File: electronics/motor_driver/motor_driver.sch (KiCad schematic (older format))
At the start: 6 parts, among them J101 CONN_02X20, J102 CONN_01X02, J103 CONN_01X02, J104 CONN_01X02

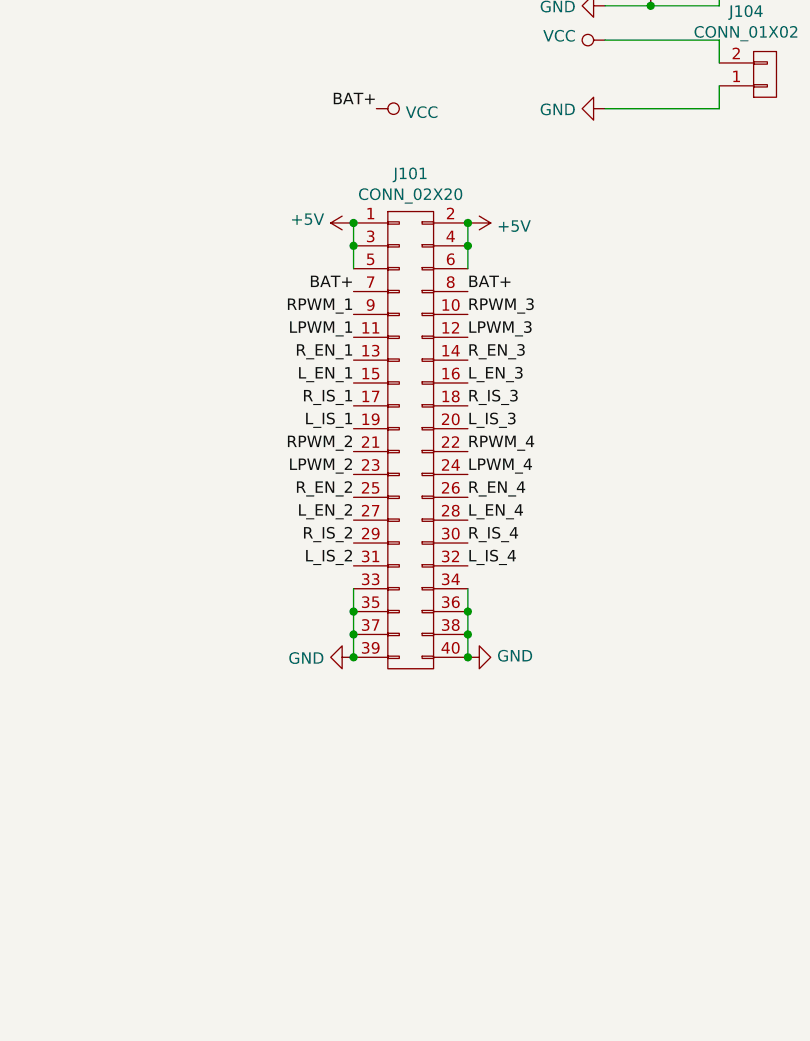
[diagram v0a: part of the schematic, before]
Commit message: Rensa + byta footprints + ändra vior + uppdatera kontakt.
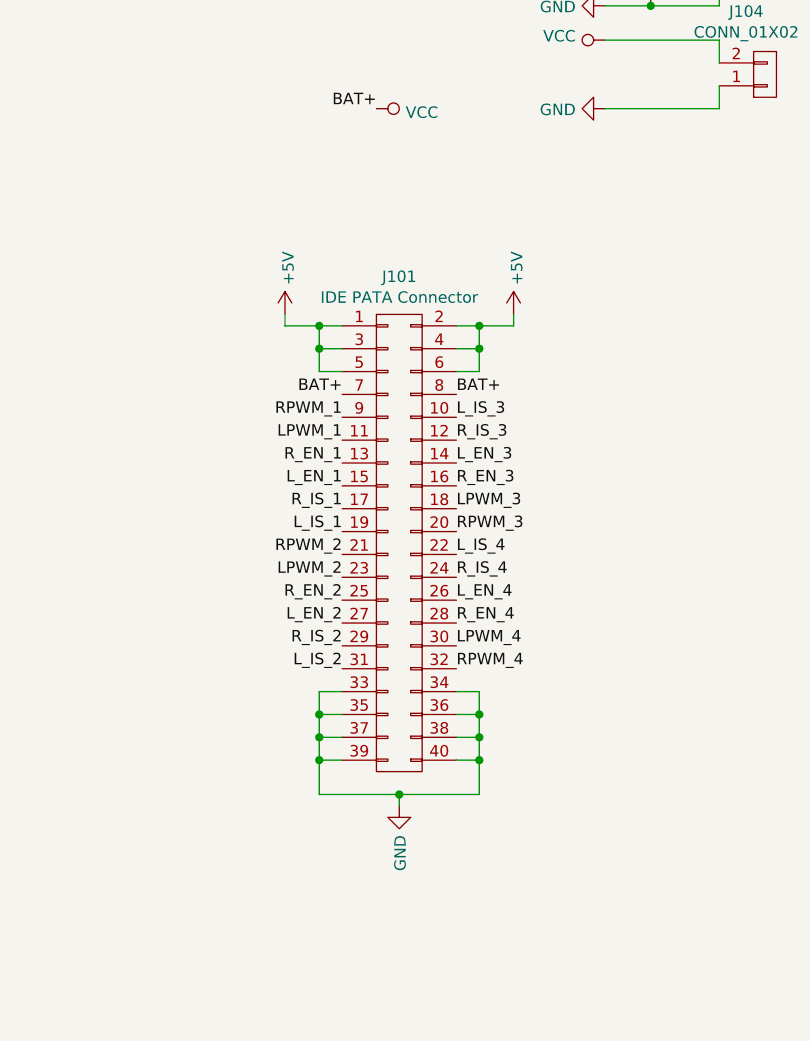
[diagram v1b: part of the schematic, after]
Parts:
- J101: value CONN_02X20 -> IDE PATA Connector
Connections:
- net LPWM_3: now also J101.18 (P18); no longer J101.12 (P12)
- net LPWM_4: now also J101.30 (P30); no longer J101.24 (P24)
- net L_EN_3: now also J101.14 (P14); no longer J101.16 (P16)
- net L_EN_4: now also J101.26 (P26); no longer J101.28 (P28)
- net L_IS_3: now also J101.10 (P10); no longer J101.20 (P20)
- net L_IS_4: now also J101.22 (P22); no longer J101.32 (P32)
- net RPWM_3: now also J101.20 (P20); no longer J101.10 (P10)
- net RPWM_4: now also J101.32 (P32); no longer J101.22 (P22)
- net R_EN_3: now also J101.16 (P16); no longer J101.14 (P14)
- net R_EN_4: now also J101.28 (P28); no longer J101.26 (P26)
- net R_IS_3: now also J101.12 (P12); no longer J101.18 (P18)
- net R_IS_4: now also J101.24 (P24); no longer J101.30 (P30)
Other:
- moved on the sheet: J101
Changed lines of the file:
@@
 L motor_driver-rescue:CONN_02X20-conn J101
 U 1 1 5CBBB8EA
-P 4350 4200
-F 0 "J101" H 4350 5365 50  0000 C CNN
-F 1 "CONN_02X20" H 4350 5274 50  0000 C CNN
-F 2 "Connectors_IDC:IDC-Header_2x20_Pitch2.54mm_Straight" H 4350 3250 50  0001 C CNN
-F 3 "" H 4350 3250 50  0001 C CNN
-	1    4350 4200
+P 4300 4650
+F 0 "J101" H 4300 5815 50  0000 C CNN
+F 1 "IDE PATA Connector" H 4300 5724 50  0000 C CNN
+F 2 "Connectors_IDC:IDC-Header_2x20_Pitch2.54mm_Straight" H 4300 3700 50  0001 C CNN
+F 3 "" H 4300 3700 50  0001 C CNN
+	1    4300 4650
 	1    0    0    -1
 $EndComp
@@
 L power:+5V #PWR0109
 U 1 1 5CBBB9C3
-P 4100 3250
-F 0 "#PWR0109" H 4100 3100 50  0001 C CNN
-F 1 "+5V" V 4115 3378 50  0000 L CNN
-F 2 "" H 4100 3250 50  0001 C CNN
-F 3 "" H 4100 3250 50  0001 C CNN
-	1    4100 3250
-	0    -1   -1   0
-$EndComp
-$Comp
-L power:GND #PWR0110
-U 1 1 5CBBBA24
-P 4100 5150
-F 0 "#PWR0110" H 4100 4900 50  0001 C CNN
-F 1 "GND" V 4105 5022 50  0000 R CNN
-F 2 "" H 4100 5150 50  0001 C CNN
-F 3 "" H 4100 5150 50  0001 C CNN
-	1    4100 5150
-	0    1    1    0
+P 3800 3650
+F 0 "#PWR0109" H 3800 3500 50  0001 C CNN
+F 1 "+5V" V 3815 3778 50  0000 L CNN
+F 2 "" H 3800 3650 50  0001 C CNN
+F 3 "" H 3800 3650 50  0001 C CNN
+	1    3800 3650
+	1    0    0    -1
 $EndComp
 Wire Wire Line
@@
 Text Label 2150 6450 0    50   ~ 0
 VCC_2
-Wire Wire Line
-	4100 3250 4100 3350
-Connection ~ 4100 3250
-Wire Wire Line
-	4100 3350 4100 3450
-Connection ~ 4100 3350
 $Comp
 L power:+5V #PWR0111
 U 1 1 5CBF87ED
-P 4600 3250
-F 0 "#PWR0111" H 4600 3100 50  0001 C CNN
-F 1 "+5V" V 4615 3378 50  0000 L CNN
-F 2 "" H 4600 3250 50  0001 C CNN
-F 3 "" H 4600 3250 50  0001 C CNN
-	1    4600 3250
-	0    1    1    0
-$EndComp
-Wire Wire Line
-	4600 3250 4600 3350
-Connection ~ 4600 3250
-Wire Wire Line
-	4600 3350 4600 3450
-Connection ~ 4600 3350
+P 4800 3650
+F 0 "#PWR0111" H 4800 3500 50  0001 C CNN
+F 1 "+5V" V 4815 3778 50  0000 L CNN
+F 2 "" H 4800 3650 50  0001 C CNN
+F 3 "" H 4800 3650 50  0001 C CNN
+	1    4800 3650
+	1    0    0    -1
+$EndComp
 $Comp
 L power:GND #PWR0112
 U 1 1 5CBF896C
-P 4600 5150
-F 0 "#PWR0112" H 4600 4900 50  0001 C CNN
-F 1 "GND" V 4605 5022 50  0000 R CNN
-F 2 "" H 4600 5150 50  0001 C CNN
-F 3 "" H 4600 5150 50  0001 C CNN
-	1    4600 5150
-	0    -1   -1   0
-$EndComp
-Wire Wire Line
-	4600 5150 4600 5050
-Connection ~ 4600 5150
-Wire Wire Line
-	4600 5050 4600 4950
-Connection ~ 4600 5050
-Wire Wire Line
-	4100 4950 4100 5050
-Wire Wire Line
-	4100 5050 4100 5150
-Connection ~ 4100 5050
-Connection ~ 4100 5150
-Text Label 4100 3650 2    50   ~ 0
+P 4300 5800
+F 0 "#PWR0112" H 4300 5550 50  0001 C CNN
+F 1 "GND" V 4305 5672 50  0000 R CNN
+F 2 "" H 4300 5800 50  0001 C CNN
+F 3 "" H 4300 5800 50  0001 C CNN
+	1    4300 5800
+	1    0    0    -1
+$EndComp
+Text Label 4050 4100 2    50   ~ 0
 RPWM_1
-Text Label 4100 3750 2    50   ~ 0
+Text Label 4050 4200 2    50   ~ 0
 LPWM_1
-Text Label 4100 3850 2    50   ~ 0
+Text Label 4050 4300 2    50   ~ 0
 R_EN_1
-Text Label 4100 3950 2    50   ~ 0
+Text Label 4050 4400 2    50   ~ 0
 L_EN_1
-Text Label 4100 4050 2    50   ~ 0
+Text Label 4050 4500 2    50   ~ 0
 R_IS_1
-Text Label 4100 4150 2    50   ~ 0
+Text Label 4050 4600 2    50   ~ 0
 L_IS_1
-Text Label 4100 4250 2    50   ~ 0
+Text Label 4050 4700 2    50   ~ 0
 RPWM_2
-Text Label 4100 4350 2    50   ~ 0
+Text Label 4050 4800 2    50   ~ 0
 LPWM_2
-Text Label 4100 4450 2    50   ~ 0
+Text Label 4050 4900 2    50   ~ 0
 R_EN_2
-Text Label 4100 4550 2    50   ~ 0
+Text Label 4050 5000 2    50   ~ 0
 L_EN_2
-Text Label 4100 4650 2    50   ~ 0
+Text Label 4050 5100 2    50   ~ 0
 R_IS_2
-Text Label 4100 4750 2    50   ~ 0
+Text Label 4050 5200 2    50   ~ 0
 L_IS_2
-Wire Wire Line
-	4100 4950 4100 4850
-Connection ~ 4100 4950
-Wire Wire Line
-	4600 4950 4600 4850
-Connection ~ 4600 4950
-Text Label 4600 3650 0    50   ~ 0
+Text Label 4550 4600 0    50   ~ 0
 RPWM_3
-Text Label 4600 3750 0    50   ~ 0
+Text Label 4550 4500 0    50   ~ 0
 LPWM_3
-Text Label 4600 3850 0    50   ~ 0
+Text Label 4550 4400 0    50   ~ 0
 R_EN_3
-Text Label 4600 3950 0    50   ~ 0
+Text Label 4550 4300 0    50   ~ 0
 L_EN_3
-Text Label 4600 4050 0    50   ~ 0
+Text Label 4550 4200 0    50   ~ 0
 R_IS_3
-Text Label 4600 4150 0    50   ~ 0
+Text Label 4550 4100 0    50   ~ 0
 L_IS_3
-Text Label 4600 4250 0    50   ~ 0
+Text Label 4550 5200 0    50   ~ 0
 RPWM_4
-Text Label 4600 4350 0    50   ~ 0
+Text Label 4550 5100 0    50   ~ 0
 LPWM_4
-Text Label 4600 4450 0    50   ~ 0
+Text Label 4550 5000 0    50   ~ 0
 R_EN_4
-Text Label 4600 4550 0    50   ~ 0
+Text Label 4550 4900 0    50   ~ 0
 L_EN_4
-Text Label 4600 4650 0    50   ~ 0
+Text Label 4550 4800 0    50   ~ 0
 R_IS_4
-Text Label 4600 4750 0    50   ~ 0
+Text Label 4550 4700 0    50   ~ 0
 L_IS_4
-Text Label 4100 3550 2    50   ~ 0
+Text Label 4050 4000 2    50   ~ 0
 BAT+
-Text Label 4600 3550 0    50   ~ 0
+Text Label 4550 4000 0    50   ~ 0
 BAT+
 Text Label 2150 950  0    50   ~ 0
@@
 	0    1    1    0
 $EndComp
+Wire Wire Line
+	4050 3900 3950 3900
+Wire Wire Line
+	3950 3900 3950 3800
+Wire Wire Line
+	3950 3800 4050 3800
+Wire Wire Line
+	3950 3800 3950 3700
+Wire Wire Line
+	3950 3700 4050 3700
+Connection ~ 3950 3800
+Wire Wire Line
+	3800 3650 3800 3700
+Wire Wire Line
+	3800 3700 3950 3700
+Connection ~ 3950 3700
+Wire Wire Line
+	4550 3700 4650 3700
+Wire Wire Line
+	4650 3700 4650 3800
+Wire Wire Line
+	4650 3800 4550 3800
+Wire Wire Line
+	4550 3900 4650 3900
+Wire Wire Line
+	4650 3900 4650 3800
+Connection ~ 4650 3800
+Wire Wire Line
+	4650 3700 4800 3700
+Wire Wire Line
+	4800 3700 4800 3650
+Connection ~ 4650 3700
+Wire Wire Line
+	4050 5300 3950 5300
+Wire Wire Line
+	3950 5300 3950 5400
+Wire Wire Line
+	3950 5750 4300 5750
+Wire Wire Line
+	4300 5750 4300 5800
+Wire Wire Line
+	4550 5300 4650 5300
+Wire Wire Line
+	4650 5300 4650 5400
+Wire Wire Line
+	4650 5750 4300 5750
+Connection ~ 4300 5750
+Wire Wire Line
+	4550 5600 4650 5600
+Connection ~ 4650 5600
+Wire Wire Line
+	4650 5600 4650 5750
+Wire Wire Line
+	4650 5500 4550 5500
+Connection ~ 4650 5500
+Wire Wire Line
+	4650 5500 4650 5600
+Wire Wire Line
+	4550 5400 4650 5400
+Connection ~ 4650 5400
+Wire Wire Line
+	4650 5400 4650 5500
+Wire Wire Line
+	4050 5400 3950 5400
+Connection ~ 3950 5400
+Wire Wire Line
+	3950 5400 3950 5500
+Wire Wire Line
+	3950 5500 4050 5500
+Connection ~ 3950 5500
+Wire Wire Line
+	3950 5500 3950 5600
+Wire Wire Line
+	4050 5600 3950 5600
+Connection ~ 3950 5600
+Wire Wire Line
+	3950 5600 3950 5750
 $EndSCHEMATC
